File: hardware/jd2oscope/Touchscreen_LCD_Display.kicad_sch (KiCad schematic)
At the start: 2 parts, among them U4 ILI9341-320x240-TFT-Touch

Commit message: feat: screen implemented
alongside screen implementation, re-structured layout for schematics, and cleaned up SPI comm. conn.s; also implemented ADC module successfully (sans SPI section for it; that comes next)
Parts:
- R1: footprint (none) -> Resistor_SMD:R_0603_1608Metric_Pad0.98x0.95mm_HandSolder
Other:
- note added: "Note: these pins are for the SD card reader; since we will not be using the SD card reader for this project, there is no need to concern ourselves with enabling its SPI comm."
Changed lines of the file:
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@@
 	(generator_version "8.0")
 	(paper "A4")
+	(polyline
+		(pts
+			(xy 102.87 97.79) (xy 104.14 97.79)
+		)
+		(stroke
+			(width 0)
+			(type default)
+		)
+	)
 	(wire
 		(pts
@@
 	(polyline
 		(pts
+			(xy 102.87 96.52) (xy 102.87 99.06)
+		)
+		(stroke
+			(width 0)
+			(type default)
+		)
+	)
+	(polyline
+		(pts
 			(xy 199.39 95.885) (xy 199.39 97.79)
+		)
+		(stroke
+			(width 0)
+			(type default)
+		)
+	)
+	(polyline
+		(pts
+			(xy 102.87 99.06) (xy 104.14 97.79)
+		)
+		(stroke
+			(width 0)
+			(type default)
+		)
+	)
+	(polyline
+		(pts
+			(xy 104.14 97.79) (xy 102.87 96.52)
+		)
+		(stroke
+			(width 0)
+			(type default)
+		)
+	)
+	(polyline
+		(pts
+			(xy 99.06 97.79) (xy 104.14 97.79)
 		)
 		(stroke
@@
 		)
 	)
+	(text "Note:\nthese pins are for the SD card reader; since\nwe will not be using the SD card reader for \nthis project, there is no need to concern\nourselves with enabling its SPI comm."
+		(exclude_from_sim no)
+		(at 55.372 96.266 0)
+		(effects
+			(font
+				(size 1.27 1.27)
+			)
+			(justify left)
+		)
+	)
 	(hierarchical_label "5V"
 		(shape input)
 		(at 191.77 97.79 0)
+		(fields_autoplaced yes)
 		(effects
 			(font
@@
 		(shape passive)
 		(at 163.83 82.55 0)
+		(fields_autoplaced yes)
 		(effects
 			(font
@@
 		(shape input)
 		(at 163.83 80.01 0)
+		(fields_autoplaced yes)
 		(effects
 			(font
@@
 			)
 		)
+		(property "Sim.Device" ""
+			(at 127 90.17 0)
+			(effects
+				(font
+					(size 1.27 1.27)
+				)
+				(hide yes)
+			)
+		)
+		(property "Sim.Params" ""
+			(at 127 90.17 0)
+			(effects
+				(font
+					(size 1.27 1.27)
+				)
+				(hide yes)
+			)
+		)
+		(property "Sim.Pins" ""
+			(at 127 90.17 0)
+			(effects
+				(font
+					(size 1.27 1.27)
+				)
+				(hide yes)
+			)
+		)
+		(property "Sim.Type" ""
+			(at 127 90.17 0)
+			(effects
+				(font
+					(size 1.27 1.27)
+				)
+				(hide yes)
+			)
+		)
 		(pin ""
 		)
@@
 			)
 		)
-		(property "Footprint" ""
+		(property "Footprint" "Resistor_SMD:R_0603_1608Metric_Pad0.98x0.95mm_HandSolder"
 			(at 187.96 99.568 90)
 			(effects
@@
 			(at 187.96 97.79 0)
 			(effects
+				(font
+					(size 1.27 1.27)
+				)
+				(hide yes)
+			)
+		)
+		(property "Sim.Device" ""
+			(at 187.96 97.79 0)
+			(effects
+				(font
+					(size 1.27 1.27)
+				)
+				(hide yes)
+			)
+		)
+		(property "Sim.Params" ""
+			(at 187.96 97.79 0)
+			(effects
+				(font
+					(size 1.27 1.27)
+				)
+				(hide yes)
+			)
+		)
+		(property "Sim.Pins" ""
+			(at 187.96 97.79 0)
+			(effects
+				(font
+					(size 1.27 1.27)
+				)
+				(hide yes)
+			)
+		)
+		(property "Sim.Type" ""
+			(at 187.96 97.79 0)
+			(effects

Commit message: feat: lot of progress
added decoupling caps, implemented a lot more of the comm. protocol stuffs, updated BNC connector to updated version, added more notes for GPIO pin I/O for future code implementation, lot of other stuff too (frankly can't remember all of it lol); I commit here b/c want to back up progress b/4 I go get smth to eat ;)
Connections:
- no-connect marks 0 -> 4
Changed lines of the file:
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@@
 	(generator_version "8.0")
 	(paper "A4")
+	(no_connect
+		(at 107.95 92.71)
+	)
+	(no_connect
+		(at 107.95 100.33)
+	)
+	(no_connect
+		(at 107.95 95.25)
+	)
+	(no_connect
+		(at 107.95 97.79)
+	)
 	(polyline
 		(pts
@@
 		(shape input)
 		(at 191.77 97.79 0)
-		(fields_autoplaced yes)
 		(effects
 			(font
@@
 		(shape passive)
 		(at 163.83 82.55 0)
-		(fields_autoplaced yes)
 		(effects
 			(font
@@
 		(shape input)
 		(at 163.83 80.01 0)
-		(fields_autoplaced yes)
-		(effects
-			(font
+		(effects
+			(font

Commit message: feat: more stuff added
yep
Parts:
- U4: footprint (none) -> Display:CR2013-MI2120
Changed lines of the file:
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@@
 			)
 		)
-		(property "Footprint" ""
+		(property "Footprint" "Display:CR2013-MI2120"
 			(at 126.746 70.866 0)
 			(effects
@@
 		)
 		(property "Sim.Type" ""
+			(at 127 90.17 0)
+			(effects
+				(font
+					(size 1.27 1.27)
+				)
+				(hide yes)
+			)
+		)
+		(property "Comment" ""
+			(at 127 90.17 0)
+			(effects
+				(font
+					(size 1.27 1.27)
+				)
+				(hide yes)
+			)
+		)
+		(property "EU_RoHS_Compliance" ""
+			(at 127 90.17 0)
+			(effects
+				(font
+					(size 1.27 1.27)
+				)
+				(hide yes)
+			)
+		)
+		(property "Number_of_Positions" ""
 			(at 127 90.17 0)
 			(effects
@@
 			(at 187.96 97.79 0)
 			(effects
+				(font
+					(size 1.27 1.27)
+				)
+				(hide yes)
+			)
+		)
+		(property "Comment" ""
+			(at 187.96 97.79 0)
+			(effects
+				(font
+					(size 1.27 1.27)
+				)
+				(hide yes)
+			)
+		)
+		(property "EU_RoHS_Compliance" ""
+			(at 187.96 97.79 0)
+			(effects
+				(font
+					(size 1.27 1.27)
+				)
+				(hide yes)
+			)
+		)
+		(property "Number_of_Positions" ""
+			(at 187.96 97.79 0)
+			(effects

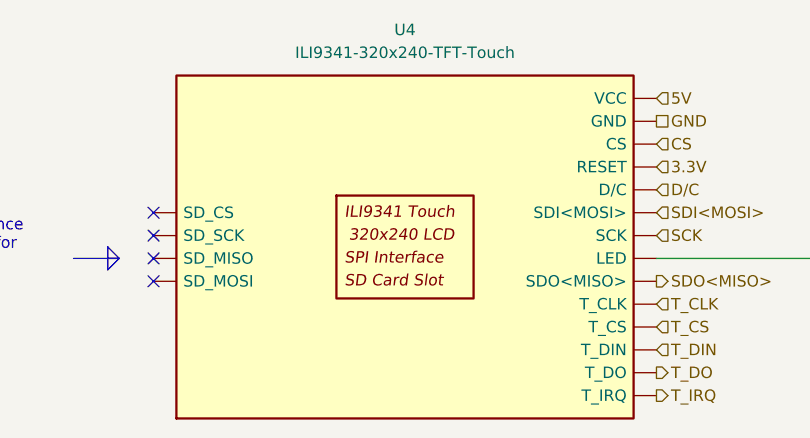
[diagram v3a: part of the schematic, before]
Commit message: fix: ERC funtimes
fixed a bunch of dependencies with ERC checks for the schematic; shouuuuld be easier/actually possible to open on other devices now?? (added a buncha schematics & footprints to the local files & whatnot)
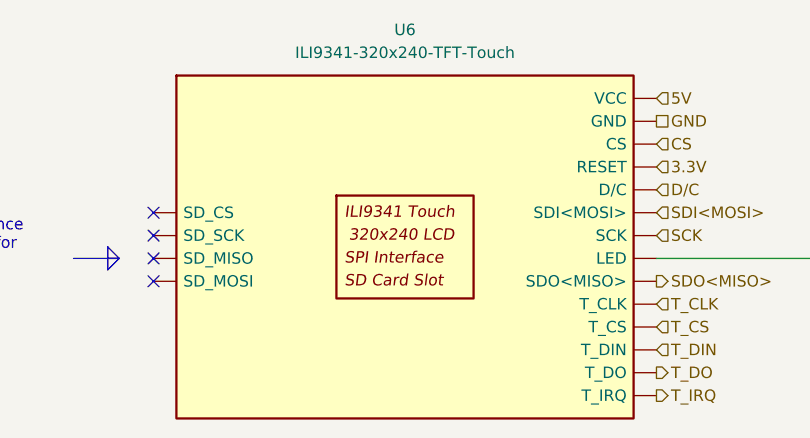
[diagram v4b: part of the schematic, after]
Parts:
- removed U4: ILI9341-320x240-TFT-Touch, Display:CR2013-MI2120, symbol lockBuster:ILI9341-320x240-TFT-Touch
- added U6: ILI9341-320x240-TFT-Touch, jd2Oscope_Footprints:CR2013-MI2120, symbol ILI9341_Touchscreen:ILI9341-320x240-TFT-Touch
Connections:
- net 3.3V: now also U6. (VCC)
- net 5V: now also U6. (VCC)
- net CS: now also U6. (VCC)
- net D/C: now also U6. (VCC)
- net GND: now also U6. (VCC)
- net SCK: now also U6. (VCC)
- net SDI<MOSI>: now also U6. (VCC)
- net SDO<MISO>: now also U6. (VCC)
- net T_CLK: now also U6. (VCC)
- net T_CS: now also U6. (VCC)
- net T_DIN: now also U6. (VCC)
- net T_DO: now also U6. (VCC)
- net T_IRQ: now also U6. (VCC)
- net at R1.1: now also U6. (VCC)
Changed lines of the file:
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@@
 	)
 	(symbol
-		(lib_id "lockBuster:ILI9341-320x240-TFT-Touch")
+		(lib_name "ILI9341_Touchscreen:ILI9341-320x240-TFT-Touch")
+		(lib_id "ILI9341_Touchscreen:ILI9341-320x240-TFT-Touch")
 		(at 127 90.17 0)
 		(unit 1)
@@
 		(dnp no)
 		(fields_autoplaced yes)
-		(property "Reference" "U4"
+		(property "Reference" "U6"
 			(at 135.89 72.39 0)
 			(effects
@@
 			)
 		)
-		(property "Footprint" "Display:CR2013-MI2120"
+		(property "Footprint" "jd2Oscope_Footprints:CR2013-MI2120"
 			(at 126.746 70.866 0)
 			(effects
@@
 			(project ""
 				(path "/eb18a3da-9fbf-4329-a814-1afab785c817/90e44cf6-9696-4eec-a87b-3c33baa89c99"
-					(reference "U4")
+					(reference "U6")
 					(unit 1)
 				)

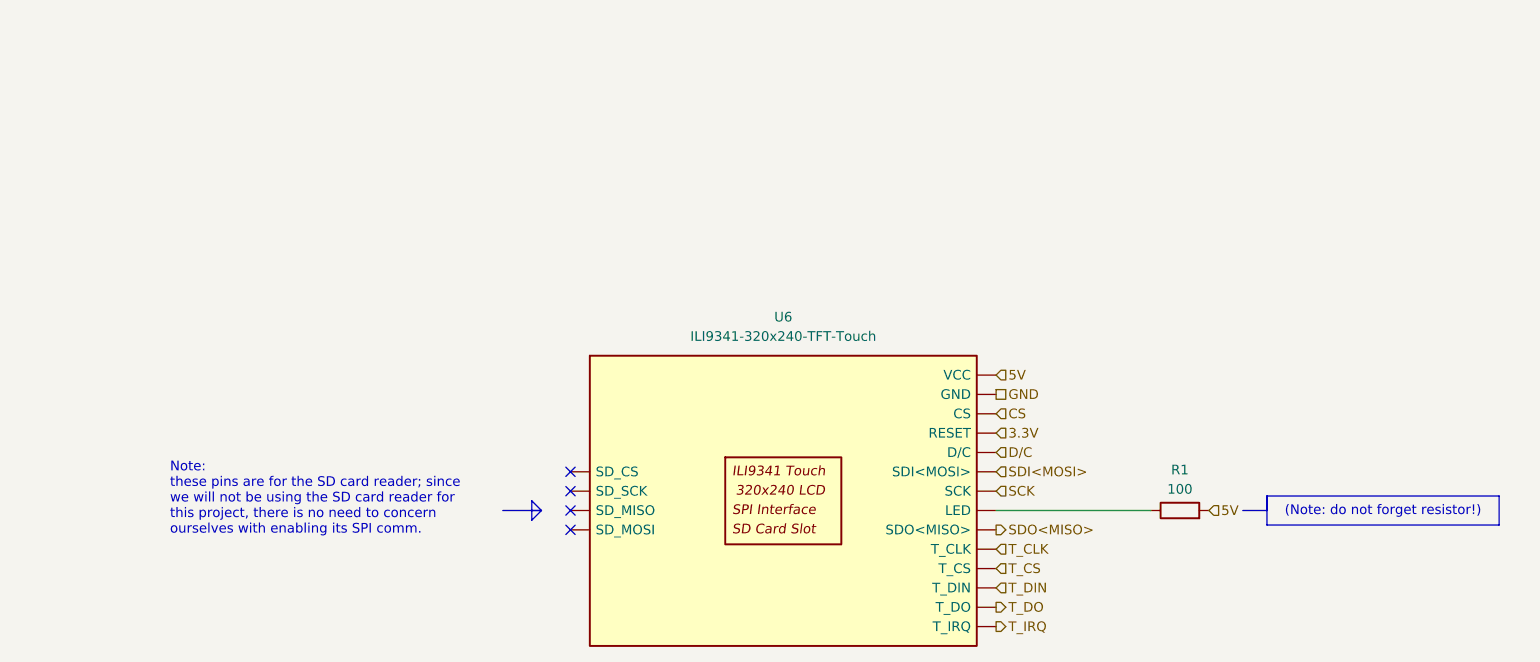
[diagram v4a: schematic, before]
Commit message: fix: footprint/symbol fixes for ILI9341_Touch
blegh
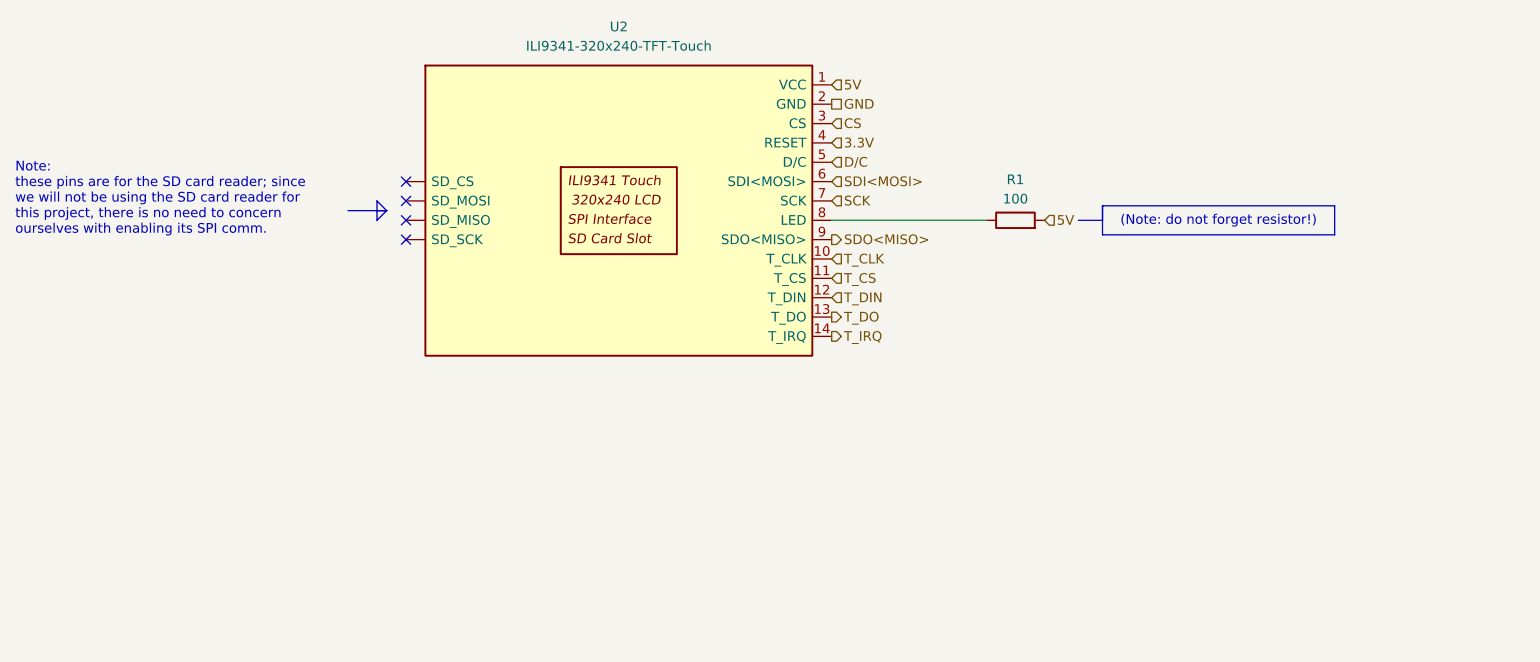
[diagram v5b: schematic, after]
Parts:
- removed U6: ILI9341-320x240-TFT-Touch, jd2Oscope_Footprints:CR2013-MI2120, symbol ILI9341_Touchscreen:ILI9341-320x240-TFT-Touch
- added U2: ILI9341-320x240-TFT-Touch, Connector_PinHeader_2.54mm:PinHeader_1x14_P2.54mm_Vertical, symbol ILI9341:ILI9341-320x240-TFT-Touch
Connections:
- net 3.3V: now also U2.4 (RESET)
- net 5V: now also U2.1 (VCC)
- net CS: now also U2.3 (CS)
- net D/C: now also U2.5 (D/C)
- net GND: now also U2.2 (GND)
- net SCK: now also U2.7 (SCK)
- net SDI<MOSI>: now also U2.6 (SDI<MOSI>)
- net SDO<MISO>: now also U2.9 (SDO<MISO>)
- net T_CLK: now also U2.10 (T_CLK)
- net T_CS: now also U2.11 (T_CS)
- net T_DIN: now also U2.12 (T_DIN)
- net T_DO: now also U2.13 (T_DO)
- net T_IRQ: now also U2.14 (T_IRQ)
- net at R1.1: now also U2.8 (LED)
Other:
- moved on the sheet: R1

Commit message: feat: ERC is now happy!
We now pass all ERC checks in terms of errors; it is now fully satisfied!! (and, any warnings are just due to the fact that we made local edits to global symbol values, so we're ballin' all the way frfr)
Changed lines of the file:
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@@
 	)
 	(hierarchical_label "SDO<MISO>"
-		(shape output)
+		(shape tri_state)
 		(at 142.24 62.23 0)
 		(effects
@@
 	)
 	(hierarchical_label "T_DO"
-		(shape output)
+		(shape tri_state)
 		(at 142.24 72.39 0)
 		(effects
@@
 		(shape input)
 		(at 142.24 49.53 0)
-		(fields_autoplaced yes)
 		(effects
 			(font
@@
 			(justify left)
 		)
-		(property "Netclass" ""
-			(at 142.24 50.8 0)
-			(effects
-				(font
-					(size 1.27 1.27)
-					(italic yes)
-				)
-				(justify left)
-			)
-		)
 	)

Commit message: feat/fix: no more errors for PCB import too!
Now both the ERC, and the schematic import (and my OCD) are completely satisfied, and we can dev the actual PCB; let's go!! :D
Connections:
- no-connect marks 4 -> 0
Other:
- note removed: "Note: these pins are for the SD card reader; since we will not be using the SD card reader for this project, there is no need to concern ourselves with enabling its SPI comm."
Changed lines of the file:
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@@
 	(generator_version "8.0")
 	(paper "A4")
-	(no_connect
-		(at 86.36 54.61)
-	)
-	(no_connect
-		(at 86.36 62.23)
-	)
-	(no_connect
-		(at 86.36 57.15)
-	)
-	(no_connect
-		(at 86.36 59.69)
-	)
-	(polyline
+	(wire
 		(pts
-			(xy 82.55 58.42) (xy 83.82 58.42)
+			(xy 142.24 59.69) (xy 162.56 59.69)
 		)
 		(stroke
@@
 		)
 	)
-	(wire
-		(pts
-			(xy 142.24 59.69) (xy 162.56 59.69)
-		)
-		(stroke
-			(width 0)
-			(type default)
-		)
-	)
-	(polyline
-		(pts
-			(xy 82.55 57.15) (xy 82.55 59.69)
-		)
-		(stroke
-			(width 0)
-			(type default)
-		)
-	)
 	(polyline
 		(pts
 			(xy 177.8 57.785) (xy 177.8 59.69)
-		)
-		(stroke
-			(width 0)
-			(type default)
-		)
-	)
-	(polyline
-		(pts
-			(xy 82.55 59.69) (xy 83.82 58.42)
-		)
-		(stroke
-			(width 0)
-			(type default)
-		)
-	)
-	(polyline
-		(pts
-			(xy 83.82 58.42) (xy 82.55 57.15)
-		)
-		(stroke
-			(width 0)
-			(type default)
-		)
-	)
-	(polyline
-		(pts
-			(xy 78.74 58.42) (xy 83.82 58.42)
 		)
 		(stroke
@@
 				(size 1.27 1.27)
 			)
-		)
-	)
-	(text "Note:\nthese pins are for the SD card reader; since\nwe will not be using the SD card reader for \nthis project, there is no need to concern\nourselves with enabling its SPI comm."
-		(exclude_from_sim no)
-		(at 35.052 56.896 0)
-		(effects
-			(font
-				(size 1.27 1.27)
-			)
-			(justify left)
 		)
 	)
@@
 			)
 		)
-		(pin ""
-		)
 		(pin "11"
 		)
@@
 		(pin "13"
 		)
-		(pin ""
-		)
-		(pin ""
-		)
-		(pin ""
-		)
 		(instances

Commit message: feat:net lists & net classes implemented
labeled e/a net w/ net labels to clarify nodes, & created net classes w/ desired dimensions for traces; next up is assigning net classes to e/a net & using it to create the pcb!
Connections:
- net ScreenLED_ScreenLEDres: now reaches R1.1, U2.8 (LED)
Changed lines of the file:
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@@
+		)
+	)
+	(label "ScreenLED_ScreenLEDres"
+		(at 158.75 59.69 90)
+		(effects
+			(font
+				(size 1.27 1.27)
+			)
+			(justify left bottom)
 		)
 	)
